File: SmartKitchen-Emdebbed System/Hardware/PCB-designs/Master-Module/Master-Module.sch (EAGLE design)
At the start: 12 parts, among them IC2 7805DT, J1 RJ11-2L-B, J2 RJ11-2L-B, J3 RJ11-2L-B, X1 K375M

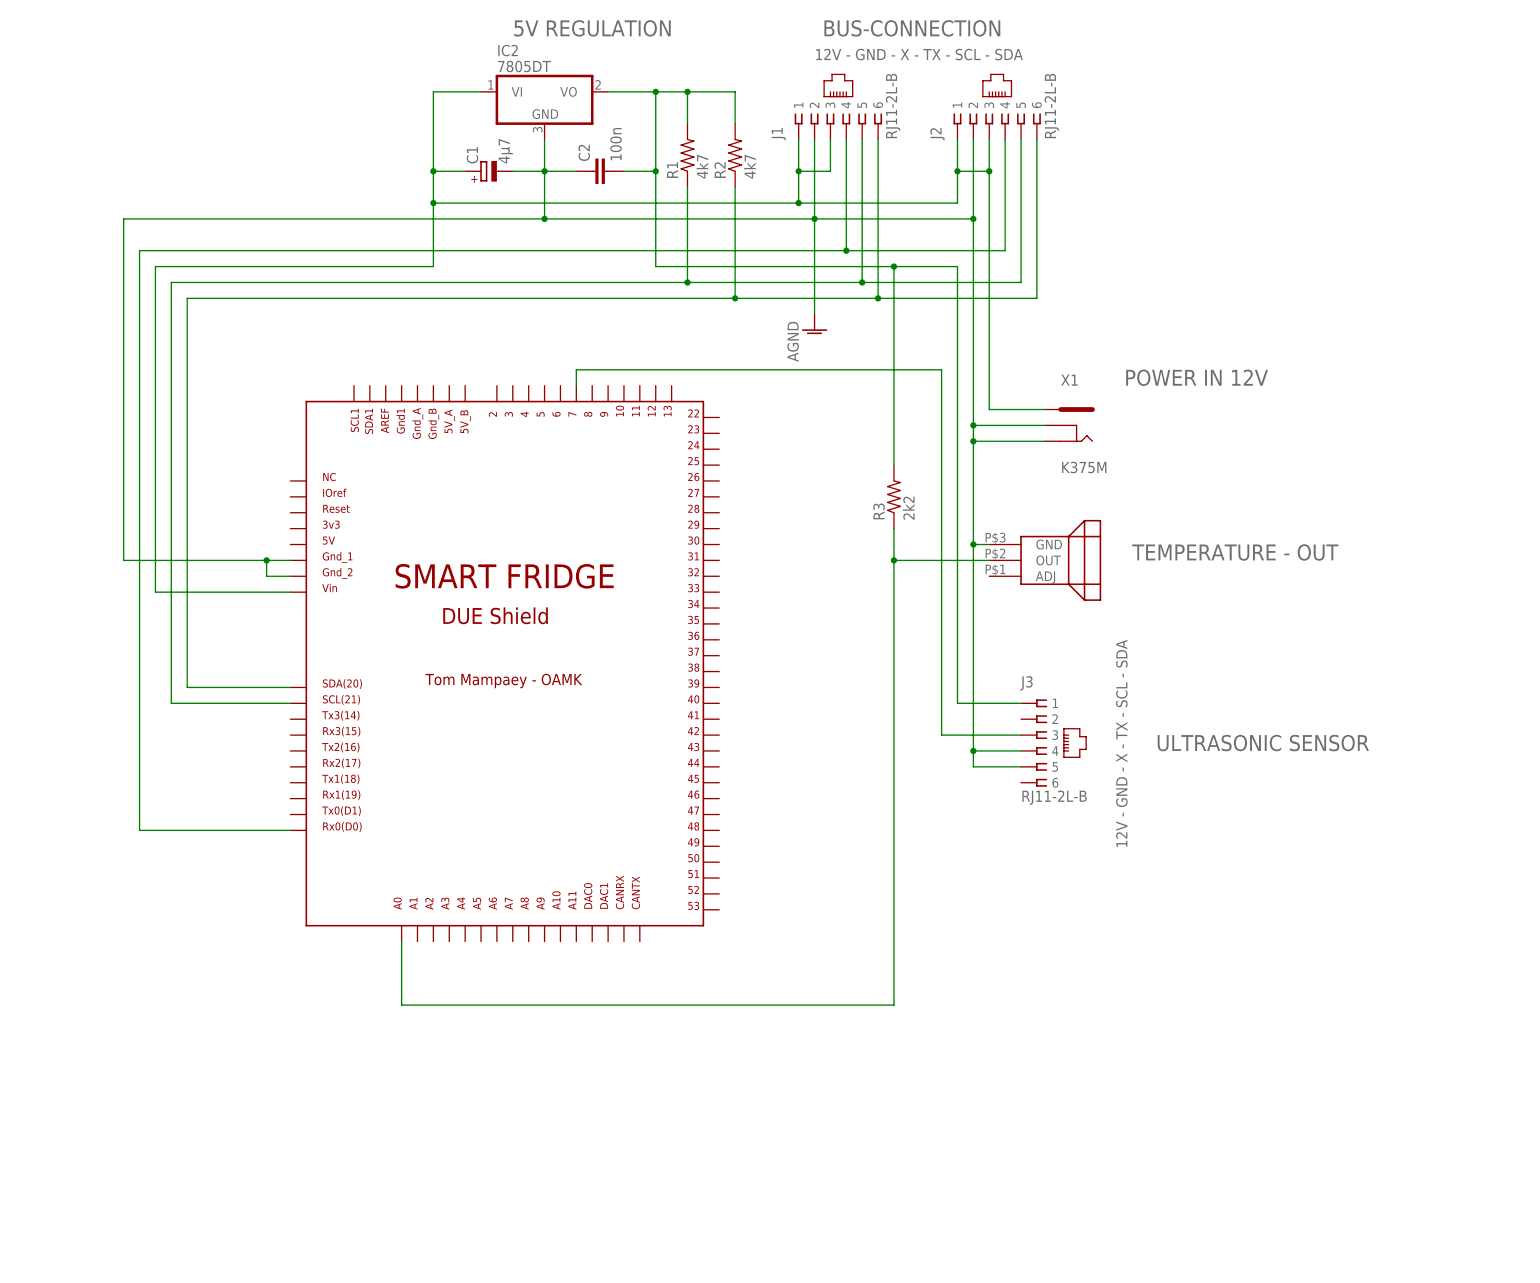
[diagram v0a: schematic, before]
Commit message: Finnishing DUE shield
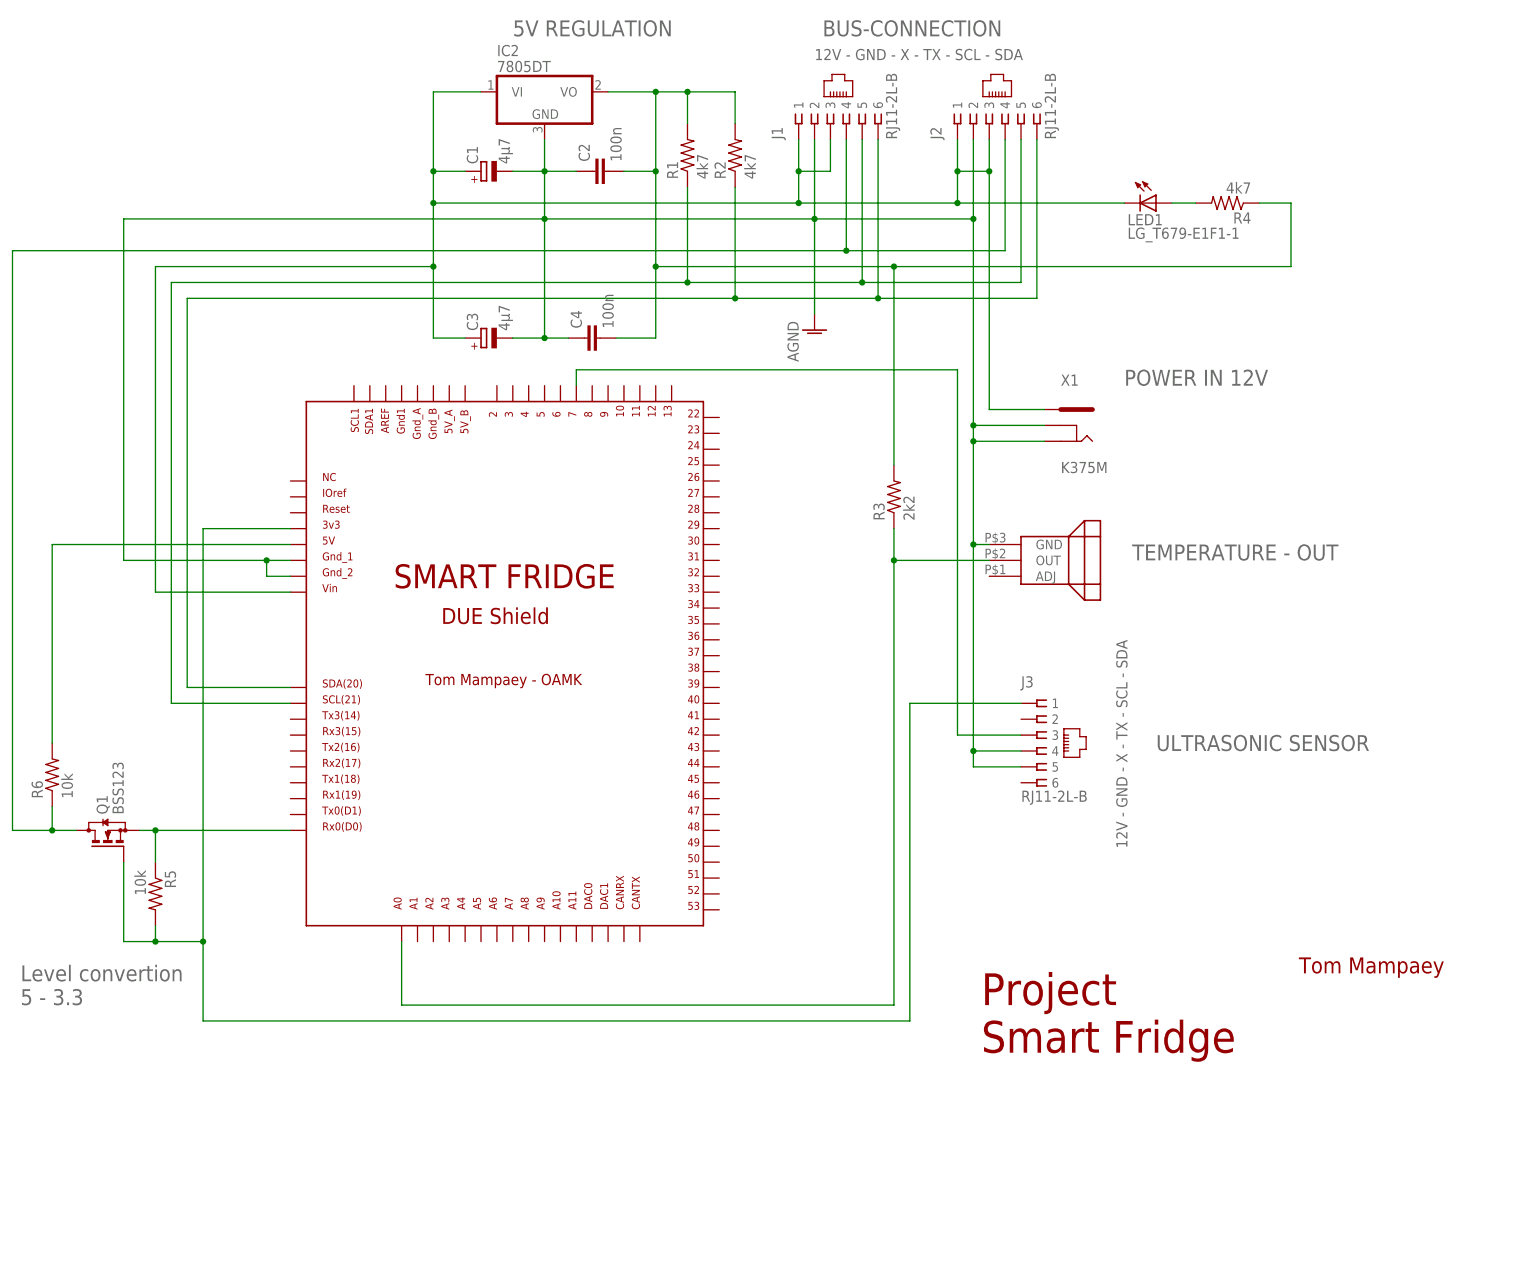
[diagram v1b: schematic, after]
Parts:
- added C3: 4µ7, resistor:CPOL-EUB
- added C4: 100n, resistor:C-EUC0603
- added LED1: LG_T679-E1F1-1, led:LG_T679-E1F1-1
- added Q1: BSS123, transistor-small-signal:BSS123
- added R4: 4k7, rcl:R-US_R0402
- added R5, R6: 10k, rcl:R-US_R0402
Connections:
- new net N$14: J3.1, Q1.G, R5.2, U$1.3V3
- new net N$7: LED1.A, R4.2
- new net N$8: C2.2, C4.2, IC2.VO, R1.2, R2.2, R3.2, R4.1
- new net N$9: Q1.S, R5.1, U$1.RX0
- net AGND: now also C3.-, C4.1
- net N$10: now also C3.+, LED1.C
- net N$2: now also Q1.D, R6.1; no longer U$1.RX0
- net N$4: now also R6.2, U$1.5V; no longer C2.2, IC2.VO, J3.1, R1.2, R2.2, R3.2
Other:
- note added: "Level convertion 5 - 3.3"
- note added: "Project Smart Fridge"
- note added: "Tom Mampaey"
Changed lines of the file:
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@@
 <part name="R3" library="rcl" deviceset="R-US_" device="R0402" value="2k2"/>
 <part name="U$2" library="LM335" deviceset="LM335" device=""/>
+<part name="LED1" library="led" deviceset="*_T679-?-1" device="E1F1" technology="LG"/>
+<part name="R4" library="rcl" deviceset="R-US_" device="R0402" value="4k7"/>
+<part name="C3" library="resistor" deviceset="CPOL-EU" device="B" value="4µ7"/>
+<part name="C4" library="resistor" deviceset="C-EU" device="C0603" value="100n"/>
+<part name="Q1" library="transistor-small-signal" deviceset="BSS123" device=""/>
+<part name="R5" library="rcl" deviceset="R-US_" device="R0402" value="10k"/>
+<part name="R6" library="rcl" deviceset="R-US_" device="R0402" value="10k"/>
 </parts>
 <sheets>
@@
 <text x="185.42" y="87.63" size="2.54" layer="95">ULTRASONIC SENSOR</text>
 <text x="181.61" y="118.11" size="2.54" layer="95">TEMPERATURE - OUT</text>
+<text x="3.81" y="46.99" size="2.54" layer="95">Level convertion
+5 - 3.3</text>
+<text x="208.28" y="52.07" size="2.54" layer="94">Tom Mampaey</text>
+<text x="157.48" y="39.37" size="5.08" layer="94">Project
+Smart Fridge</text>
 </plain>
 <instances>
@@
 <instance part="R3" gate="G$1" x="143.51" y="128.27" rot="R90"/>
 <instance part="U$2" gate="G$1" x="168.91" y="118.11"/>
+<instance part="LED1" gate="G$1" x="185.42" y="175.26" rot="R270"/>
+<instance part="R4" gate="G$1" x="196.85" y="175.26" rot="R180"/>
+<instance part="C3" gate="G$1" x="77.47" y="153.67" rot="R90"/>
+<instance part="C4" gate="G$1" x="93.98" y="153.67" rot="R90"/>
+<instance part="Q1" gate="G$1" x="17.78" y="74.93" rot="R90"/>
+<instance part="R5" gate="G$1" x="25.4" y="64.77" rot="R270"/>
+<instance part="R6" gate="G$1" x="8.89" y="83.82" rot="R90"/>
 </instances>
 <busses>
@@
 <wire x1="46.99" y1="113.03" x2="25.4" y2="113.03" width="0.1524" layer="91"/>
 <wire x1="69.85" y1="165.1" x2="25.4" y2="165.1" width="0.1524" layer="91"/>
+<pinref part="C3" gate="G$1" pin="+"/>
+<wire x1="74.93" y1="153.67" x2="69.85" y2="153.67" width="0.1524" layer="91"/>
+<wire x1="69.85" y1="153.67" x2="69.85" y2="165.1" width="0.1524" layer="91"/>
+<junction x="69.85" y="165.1"/>
+<pinref part="LED1" gate="G$1" pin="C"/>
+<wire x1="180.34" y1="175.26" x2="153.67" y2="175.26" width="0.1524" layer="91"/>
+<junction x="153.67" y="175.26"/>
 </segment>
 </net>
@@
 <segment>
 <pinref part="J2" gate="G$1" pin="4"/>
-<wire x1="22.86" y1="167.64" x2="135.89" y2="167.64" width="0.1524" layer="91"/>
+<wire x1="2.54" y1="167.64" x2="135.89" y2="167.64" width="0.1524" layer="91"/>
 <wire x1="135.89" y1="167.64" x2="161.29" y2="167.64" width="0.1524" layer="91"/>
 <wire x1="161.29" y1="167.64" x2="161.29" y2="185.42" width="0.1524" layer="91"/>
@@
 <wire x1="135.89" y1="185.42" x2="135.89" y2="167.64" width="0.1524" layer="91"/>
 <junction x="135.89" y="167.64"/>
-<wire x1="22.86" y1="167.64" x2="22.86" y2="74.93" width="0.1524" layer="91"/>
-<wire x1="46.99" y1="74.93" x2="22.86" y2="74.93" width="0.1524" layer="91"/>
-<pinref part="U$1" gate="G$1" pin="RX0"/>
+<wire x1="2.54" y1="167.64" x2="2.54" y2="74.93" width="0.1524" layer="91"/>
+<pinref part="Q1" gate="G$1" pin="D"/>
+<pinref part="R6" gate="G$1" pin="1"/>
+<wire x1="12.7" y1="74.93" x2="8.89" y2="74.93" width="0.1524" layer="91"/>
+<wire x1="8.89" y1="74.93" x2="8.89" y2="78.74" width="0.1524" layer="91"/>
+<wire x1="2.54" y1="74.93" x2="8.89" y2="74.93" width="0.1524" layer="91"/>
+<junction x="8.89" y="74.93"/>
 </segment>
 </net>
@@
 <wire x1="156.21" y1="85.09" x2="156.21" y2="87.63" width="0.1524" layer="91"/>
 <junction x="156.21" y="87.63"/>
+<pinref part="C4" gate="G$1" pin="1"/>
+<wire x1="91.44" y1="153.67" x2="87.63" y2="153.67" width="0.1524" layer="91"/>
+<wire x1="87.63" y1="153.67" x2="87.63" y2="172.72" width="0.1524" layer="91"/>
+<pinref part="C3" gate="G$1" pin="-"/>
+<wire x1="82.55" y1="153.67" x2="87.63" y2="153.67" width="0.1524" layer="91"/>
+<junction x="87.63" y="153.67"/>
 </segment>
 </net>
@@
 <segment>
 <pinref part="J3" gate="G$1" pin="3"/>
-<wire x1="163.83" y1="90.17" x2="151.13" y2="90.17" width="0.1524" layer="91"/>
-<wire x1="151.13" y1="90.17" x2="151.13" y2="148.59" width="0.1524" layer="91"/>
-<wire x1="151.13" y1="148.59" x2="92.71" y2="148.59" width="0.1524" layer="91"/>
+<wire x1="163.83" y1="90.17" x2="153.67" y2="90.17" width="0.1524" layer="91"/>
+<wire x1="153.67" y1="90.17" x2="153.67" y2="148.59" width="0.1524" layer="91"/>
+<wire x1="153.67" y1="148.59" x2="92.71" y2="148.59" width="0.1524" layer="91"/>
 <pinref part="U$1" gate="G$1" pin="7"/>
 <wire x1="92.71" y1="148.59" x2="92.71" y2="146.05" width="0.1524" layer="91"/>
 </segment>
 </net>
-<net name="N$4" class="0">
-<segment>
+<net name="N$7" class="0">
+<segment>
+<pinref part="R4" gate="G$1" pin="2"/>
+<pinref part="LED1" gate="G$1" pin="A"/>
+<wire x1="191.77" y1="175.26" x2="187.96" y2="175.26" width="0.1524" layer="91"/>
+</segment>
+</net>
+<net name="N$8" class="0">
+<segment>
+<pinref part="R4" gate="G$1" pin="1"/>
+<wire x1="201.93" y1="175.26" x2="207.01" y2="175.26" width="0.1524" layer="91"/>
+<wire x1="207.01" y1="175.26" x2="207.01" y2="165.1" width="0.1524" layer="91"/>
 <pinref part="IC2" gate="A1" pin="VO"/>
 <wire x1="97.79" y1="193.04" x2="105.41" y2="193.04" width="0.1524" layer="91"/>
@@
 <pinref part="R3" gate="G$1" pin="2"/>
 <wire x1="143.51" y1="133.35" x2="143.51" y2="165.1" width="0.1524" layer="91"/>
-<pinref part="J3" gate="G$1" pin="1"/>
-<wire x1="163.83" y1="95.25" x2="153.67" y2="95.25" width="0.1524" layer="91"/>
-<wire x1="153.67" y1="95.25" x2="153.67" y2="165.1" width="0.1524" layer="91"/>
-<wire x1="153.67" y1="165.1" x2="143.51" y2="165.1" width="0.1524" layer="91"/>
 <wire x1="105.41" y1="165.1" x2="143.51" y2="165.1" width="0.1524" layer="91"/>
 <junction x="143.51" y="165.1"/>
+<wire x1="207.01" y1="165.1" x2="143.51" y2="165.1" width="0.1524" layer="91"/>
+<pinref part="C4" gate="G$1" pin="2"/>
+<wire x1="99.06" y1="153.67" x2="105.41" y2="153.67" width="0.1524" layer="91"/>
+<wire x1="105.41" y1="153.67" x2="105.41" y2="165.1" width="0.1524" layer="91"/>
+<junction x="105.41" y="165.1"/>
+</segment>
+</net>
+<net name="N$9" class="0">
+<segment>
+<pinref part="Q1" gate="G$1" pin="S"/>
+<pinref part="R5" gate="G$1" pin="1"/>
+<wire x1="22.86" y1="74.93" x2="25.4" y2="74.93" width="0.1524" layer="91"/>
+<wire x1="25.4" y1="74.93" x2="25.4" y2="69.85" width="0.1524" layer="91"/>
+<pinref part="U$1" gate="G$1" pin="RX0"/>
+<wire x1="46.99" y1="74.93" x2="25.4" y2="74.93" width="0.1524" layer="91"/>
+<junction x="25.4" y="74.93"/>
+</segment>
+</net>
+<net name="N$14" class="0">
+<segment>
+<pinref part="R5" gate="G$1" pin="2"/>
+<wire x1="25.4" y1="57.15" x2="25.4" y2="59.69" width="0.1524" layer="91"/>
+<wire x1="20.32" y1="57.15" x2="25.4" y2="57.15" width="0.1524" layer="91"/>
+<pinref part="Q1" gate="G$1" pin="G"/>
+<wire x1="20.32" y1="69.85" x2="20.32" y2="57.15" width="0.1524" layer="91"/>
+<pinref part="J3" gate="G$1" pin="1"/>
+<wire x1="163.83" y1="95.25" x2="146.05" y2="95.25" width="0.1524" layer="91"/>
+<wire x1="146.05" y1="95.25" x2="146.05" y2="44.45" width="0.1524" layer="91"/>
+<wire x1="146.05" y1="44.45" x2="33.02" y2="44.45" width="0.1524" layer="91"/>
+<wire x1="33.02" y1="44.45" x2="33.02" y2="57.15" width="0.1524" layer="91"/>
+<pinref part="U$1" gate="G$1" pin="3V3"/>
+<wire x1="33.02" y1="57.15" x2="33.02" y2="123.19" width="0.1524" layer="91"/>
+<wire x1="33.02" y1="123.19" x2="46.99" y2="123.19" width="0.1524" layer="91"/>
+<wire x1="25.4" y1="57.15" x2="33.02" y2="57.15" width="0.1524" layer="91"/>
+<junction x="25.4" y="57.15"/>
+<junction x="33.02" y="57.15"/>
+</segment>
+</net>
+<net name="N$4" class="0">
+<segment>
+<pinref part="U$1" gate="G$1" pin="5V"/>
+<pinref part="R6" gate="G$1" pin="2"/>
+<wire x1="46.99" y1="120.65" x2="8.89" y2="120.65" width="0.1524" layer="91"/>
+<wire x1="8.89" y1="120.65" x2="8.89" y2="88.9" width="0.1524" layer="91"/>
 </segment>
 </net>
@@
 </schematic>
 </drawing>
+<compatibility>
+<note version="6.3" minversion="6.2.2" severity="warning">
+Since Version 6.2.2 text objects can contain more than one line,
+which will not be processed correctly with this version.
+</note>
+</compatibility>
 </eagle>

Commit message: Adding planes and references
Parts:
- R4: value 4k7 -> 1k
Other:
- note added: "POWER INDICATION"
- note added: "SERIAL LEVEL CONVERTION"
- note removed: "Level convertion 5 - 3.3"
- moved on the sheet: C1, C2, C3, C4, IC2, J1, J2, J3, LED1, Q1, R1, R2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

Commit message: testing
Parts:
- added J4: RJ11-2L-B, con-tycoelectronics:RJ11-2L-B
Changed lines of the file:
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@@
 <setting verticaltext="up"/>
 </settings>
-<grid distance="0.05" unitdist="inch" unit="inch" style="lines" multiple="1" display="no" altdistance="0.01" altunitdist="inch" altunit="inch"/>
+<grid distance="0.1" unitdist="inch" unit="inch" style="lines" multiple="1" display="no" altdistance="0.01" altunitdist="inch" altunit="inch"/>
 <layers>
 <layer number="1" name="Top" color="4" fill="1" visible="no" active="no"/>
@@
 <part name="R5" library="rcl" deviceset="R-US_" device="R0402" value="10k"/>
 <part name="R6" library="rcl" deviceset="R-US_" device="R0402" value="10k"/>
+<part name="J4" library="con-tycoelectronics" deviceset="RJ11" device="" technology="-2L-B"/>
 </parts>
 <sheets>
@@
 <instance part="R5" gate="G$1" x="36.83" y="33.02" rot="R270"/>
 <instance part="R6" gate="G$1" x="20.32" y="52.07" rot="R90"/>
+<instance part="J4" gate="G$1" x="176.53" y="38.1"/>
 </instances>
 <busses>
